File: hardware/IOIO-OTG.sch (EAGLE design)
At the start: 57 parts, among them Q1 IRLML2244, Q2 2N7002PW, Q3 AO3404A, U1 PIC24FJ256GB206, U14 SWITCH_SPDT, U2 TPS62133RGTT, U3 VREG_MIC5216

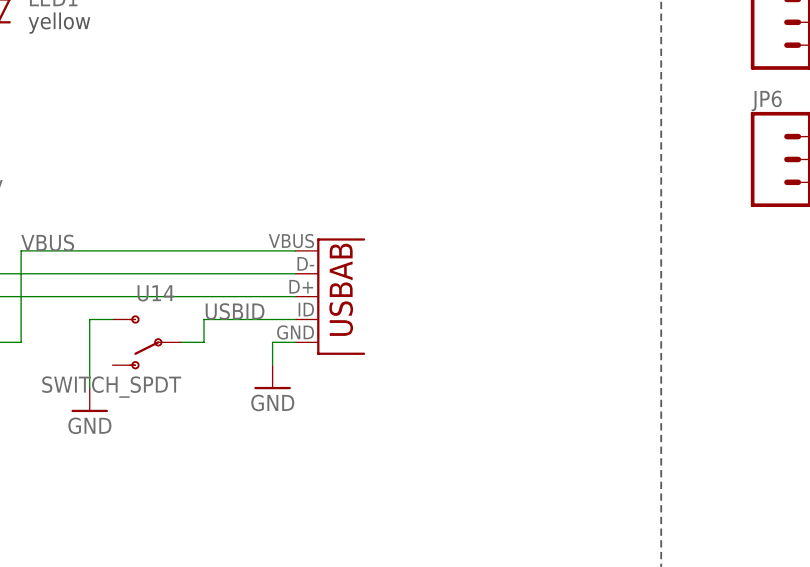
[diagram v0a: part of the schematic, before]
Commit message: Switch USB connector to part with mounting bosses
Also included an anchor polygon to strengthen mounting pads.
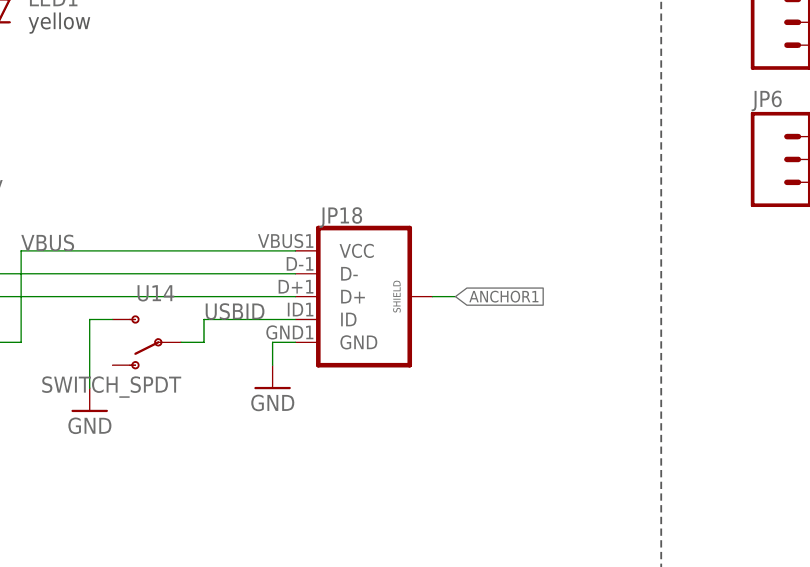
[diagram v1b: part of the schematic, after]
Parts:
- removed U$3: 10104111-0001LF, SparkFun-Connectors:USB_AB
- added JP18: (no value), SparkFun-Connectors:USB_MICROB_PLUGCONN-11752
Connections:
- new net ANCHOR1: JP18.SHIELD
- net D+: now also JP18.D+; no longer U$3.D+
- net D-: now also JP18.D-; no longer U$3.D-
- net GND: now also JP18.GND; no longer U$3.GND
- net USBID: now also JP18.ID; no longer U$3.USBID
- net VBUS: now also JP18.VCC; no longer U$3.VBUS
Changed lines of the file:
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@@
 <?xml version="1.0" encoding="utf-8"?>
 <!DOCTYPE eagle SYSTEM "eagle.dtd">
-<eagle version="6.4">
+<eagle version="7.2.0">
 <drawing>
 <settings>
@@
 <setting verticaltext="up"/>
 </settings>
-<grid distance="50" unitdist="mil" unit="mil" style="lines" multiple="1" display="yes" altdistance="25" altunitdist="mil" altunit="mil"/>
+<grid distance="0.1" unitdist="inch" unit="inch" style="lines" multiple="1" display="no" altdistance="0.01" altunitdist="inch" altunit="inch"/>
 <layers>
 <layer number="1" name="Top" color="4" fill="1" visible="no" active="no"/>
@@
 <layer number="54" name="bGND_GNDA" color="1" fill="9" visible="no" active="no"/>
 <layer number="56" name="wert" color="7" fill="1" visible="no" active="no"/>
+<layer number="57" name="tCAD" color="7" fill="1" visible="no" active="no"/>
+<layer number="90" name="Modules" color="5" fill="1" visible="yes" active="yes"/>
 <layer number="91" name="Nets" color="2" fill="1" visible="yes" active="yes"/>
 <layer number="92" name="Busses" color="1" fill="1" visible="yes" active="yes"/>
@@
 <layer number="97" name="Info" color="7" fill="1" visible="yes" active="yes"/>
 <layer number="98" name="Guide" color="6" fill="1" visible="yes" active="yes"/>
+<layer number="99" name="SpiceOrder" color="7" fill="1" visible="yes" active="yes"/>
 <layer number="100" name="Muster" color="7" fill="1" visible="no" active="no"/>
 <layer number="101" name="Patch_Top" color="12" fill="4" visible="yes" active="yes"/>
@@
 <layer number="111" name="111" color="7" fill="1" visible="yes" active="yes"/>
 <layer number="112" name="tSilk" color="7" fill="1" visible="yes" active="yes"/>
+<layer number="113" name="IDFDebug" color="4" fill="1" visible="yes" active="yes"/>
 <layer number="116" name="Patch_BOT" color="9" fill="4" visible="yes" active="yes"/>
 <layer number="118" name="Rect_Pads" color="7" fill="1" visible="yes" active="yes"/>
@@
 <layer number="132" name="bAdjust" color="7" fill="1" visible="yes" active="yes"/>
 <layer number="144" name="Drill_legend" color="7" fill="1" visible="yes" active="yes"/>
+<layer number="150" name="Notes" color="7" fill="1" visible="yes" active="yes"/>
 <layer number="151" name="HeatSink" color="7" fill="1" visible="yes" active="yes"/>
 <layer number="152" name="_bDocu" color="7" fill="1" visible="yes" active="yes"/>
+<layer number="153" name="FabDoc1" color="7" fill="1" visible="yes" active="yes"/>
+<layer number="154" name="FabDoc2" color="7" fill="1" visible="yes" active="yes"/>
+<layer number="155" name="FabDoc3" color="7" fill="1" visible="yes" active="yes"/>
 <layer number="199" name="Contour" color="7" fill="1" visible="yes" active="yes"/>
 <layer number="200" name="200bmp" color="1" fill="10" visible="yes" active="yes"/>
@@
 <attribute name="AM" value="3.3uH"/>
 </part>
-<part name="U$3" library="SparkFun-Connectors" deviceset="USB_AB" device="" value="10104111-0001LF"/>
 <part name="U$8" library="SparkFun-Aesthetics" deviceset="VIN" device=""/>
 <part name="U3" library="SparkFun-PowerIC" deviceset="VREG_MIC5216" device=""/>
@@
 <part name="C9" library="SparkFun" deviceset="CAP" device="0402-CAP" value="0.1uF"/>
 <part name="GND20" library="SparkFun" deviceset="GND" device=""/>
+<part name="JP18" library="SparkFun-Connectors" deviceset="USB_MICROB_PLUG" device="CONN-11752"/>
 </parts>
 <sheets>
@@
 <attribute name="NAME" x="141.986" y="240.284" size="1.778" layer="95" rot="R180"/>
 </instance>
-<instance part="U$3" gate="G$1" x="254" y="53.34" rot="MR180"/>
 <instance part="U$8" gate="G$1" x="322.58" y="157.48"/>
 <instance part="U3" gate="G$1" x="226.06" y="228.6" smashed="yes">
@@
 <instance part="C9" gate="G$1" x="83.82" y="226.06"/>
 <instance part="GND20" gate="1" x="83.82" y="220.98" rot="MR0"/>
+<instance part="JP18" gate="G$1" x="256.54" y="53.34"/>
 </instances>
 <busses>
@@
 </segment>
 <segment>
-<pinref part="U$3" gate="G$1" pin="GND"/>
 <wire x1="248.92" y1="48.26" x2="246.38" y2="48.26" width="0.1524" layer="91"/>
 <wire x1="246.38" y1="48.26" x2="246.38" y2="45.72" width="0.1524" layer="91"/>
 <pinref part="GND18" gate="1" pin="GND"/>
+<pinref part="JP18" gate="G$1" pin="GND"/>
 </segment>
 <segment>
@@
 <pinref part="U1" gate="G$1" pin="D-/CN84/RG3"/>
 <label x="203.2" y="55.88" size="1.778" layer="95"/>
-<pinref part="U$3" gate="G$1" pin="D-"/>
+<pinref part="JP18" gate="G$1" pin="D-"/>
 </segment>
 <segment>
@@
 <pinref part="U1" gate="G$1" pin="D+/CN83/RG2"/>
 <label x="203.2" y="53.34" size="1.778" layer="95"/>
-<pinref part="U$3" gate="G$1" pin="D+"/>
+<pinref part="JP18" gate="G$1" pin="D+"/>
 </segment>
 <segment>
@@
 <net name="USBID" class="0">
 <segment>
-<pinref part="U$3" gate="G$1" pin="USBID"/>
 <wire x1="248.92" y1="50.8" x2="238.76" y2="50.8" width="0.1524" layer="91"/>
 <label x="238.76" y="50.8" size="1.778" layer="95"/>
@@
 <pinref part="U14" gate="G$1" pin="P"/>
 <wire x1="238.76" y1="48.26" x2="236.22" y2="48.26" width="0.1524" layer="91"/>
+<pinref part="JP18" gate="G$1" pin="ID"/>
 </segment>
 <segment>
@@
 <net name="VBUS" class="0">
 <segment>
-<pinref part="U$3" gate="G$1" pin="VBUS"/>
 <wire x1="248.92" y1="58.42" x2="218.44" y2="58.42" width="0.1524" layer="91"/>
 <wire x1="198.12" y1="48.26" x2="218.44" y2="48.26" width="0.1524" layer="91"/>
@@
 <label x="218.44" y="58.42" size="1.778" layer="95"/>
 <label x="203.2" y="48.26" size="1.778" layer="95"/>
+<pinref part="JP18" gate="G$1" pin="VCC"/>
 </segment>
 <segment>
@@
 </segment>
 </net>
+<net name="ANCHOR1" class="0">
+<segment>
+<pinref part="JP18" gate="G$1" pin="SHIELD"/>
+<wire x1="264.16" y1="53.34" x2="266.7" y2="53.34" width="0.1524" layer="91"/>
+<label x="266.7" y="53.34" size="1.27" layer="95" xref="yes"/>
+</segment>
+</net>

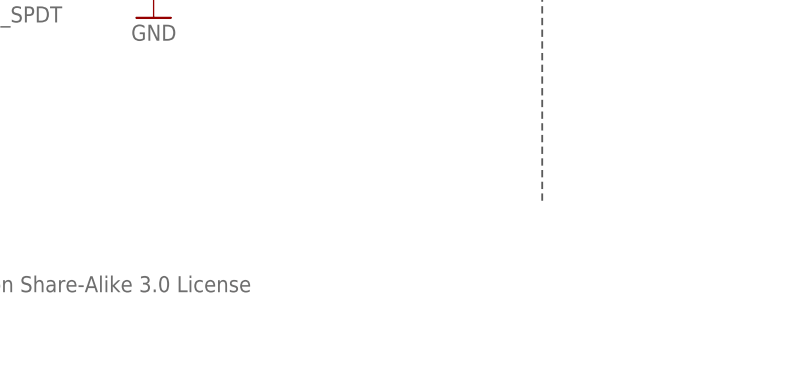
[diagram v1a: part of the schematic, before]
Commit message: Moved OSHW logo to proper device
Also moved measures to measure layer and changed units to inches
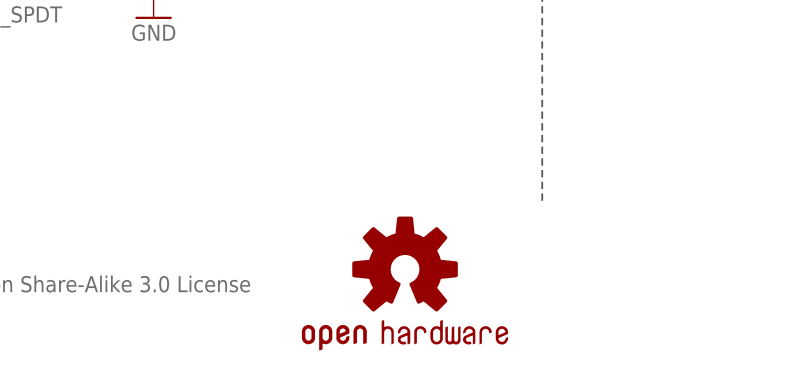
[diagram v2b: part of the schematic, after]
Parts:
- added LOGO1: OSHW-LOGOS, SparkFun-Aesthetics:OSHW-LOGOS
